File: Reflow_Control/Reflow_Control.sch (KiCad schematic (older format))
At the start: 67 parts, among them J1 Conn_5V, J2 Conn_ssr_1, J3 Conn_ssr_2, Q1 BC848, Q2 BC848, Q3 BC848, SW1 SW_Push, SW2 SW_Push, SW3 SW_Push, SW4 SW_Push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

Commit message: Kerem & Edwin dez. 20 2020 mitarbeit
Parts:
- C4: footprint PCE3853CT-ND -> Capacitor_SMD:CP_Elec_5x5.4
- H5, H6: footprint MountingHole:MountingHole_2.5mm_Pad -> owen:MountingHole_2.5mm_Pad
- SW5: footprint Rotary_Encoder:RotaryEncoder_Alps_EC11E_Vertical_H20mm -> owen:RotaryEncoder_Alps_EC11E_Vertical_H20mm
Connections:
- net BTN_A: now also U5.4 (IO0_0); no longer U5.9 (IO0_5)
- net BTN_B: now also U5.9 (IO0_5); no longer U5.10 (IO0_6)
- net BTN_CENTER: now also U5.7 (IO0_3); no longer U5.8 (IO0_4)
- net BTN_DOWN: now also U5.6 (IO0_2); no longer U5.5 (IO0_1)
- net BTN_LEFT: now also U5.5 (IO0_1); no longer U5.7 (IO0_3)
- net BTN_RIGHT: now also U5.10 (IO0_6); no longer U5.6 (IO0_2)
- net BTN_UP: now also U5.8 (IO0_4); no longer U5.4 (IO0_0)
- net INT_ENC_A: now also C10.2, R6.2, SW5.B; no longer C9.2, R5.2, SW5.A
- net INT_ENC_B: now also C9.2, R5.2, SW5.A; no longer C10.2, R6.2, SW5.B
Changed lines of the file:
@@
 EESchema Schematic File Version 4
-LIBS:Reflow_Control-cache
-EELAYER 26 0
+EELAYER 30 0
 EELAYER END
 $Descr A4 11693 8268
@@
 F 3 "" H 8500 1600 50  0001 C CNN
 	1    8500 1600
-	1    0    0    -1
-$EndComp
-$Comp
-L Device:Rotary_Encoder_Switch SW5
-U 1 1 5F6E216F
-P 10400 4350
-F 0 "SW5" H 10400 4717 50  0000 C CNN
-F 1 "Rotary_Encoder_Switch" H 10400 4626 50  0000 C CNN
-F 2 "Rotary_Encoder:RotaryEncoder_Alps_EC11E_Vertical_H20mm" H 10250 4510 50  0001 C CNN
-F 3 "~" H 10400 4610 50  0001 C CNN
-F 4 "Bourns" H 10400 4350 50  0001 C CNN "Man"
-F 5 "PEC12R-4220F-S0024" H 10400 4350 50  0001 C CNN "Man no"
-F 6 "Digikey" H 10400 4350 50  0001 C CNN "Dist"
-F 7 "PEC12R-4220F-S0024-ND" H 10400 4350 50  0001 C CNN "Dist no"
-	1    10400 4350
 	1    0    0    -1
 $EndComp
@@
 	7650 4050 7650 4150
 Connection ~ 7650 4150
+Text GLabel 1100 4400 0    50   Output ~ 0
+BTN_UP
+Text GLabel 1100 4200 0    50   Output ~ 0
+BTN_DOWN
+Text GLabel 1100 4100 0    50   Output ~ 0
+BTN_LEFT
+Text GLabel 1100 4300 0    50   Output ~ 0
+BTN_CENTER
+Text GLabel 1100 4600 0    50   Output ~ 0
+BTN_RIGHT
 Text GLabel 1100 4000 0    50   Output ~ 0
-BTN_UP
-Text GLabel 1100 4100 0    50   Output ~ 0
-BTN_DOWN
-Text GLabel 1100 4300 0    50   Output ~ 0
-BTN_LEFT
-Text GLabel 1100 4400 0    50   Output ~ 0
-BTN_CENTER
-Text GLabel 1100 4200 0    50   Output ~ 0
-BTN_RIGHT
+BTN_A
 Text GLabel 1100 4500 0    50   Output ~ 0
-BTN_A
-Text GLabel 1100 4600 0    50   Output ~ 0
 BTN_B
 $Comp
@@
 	9700 4800 9700 4900
 Connection ~ 9700 4900
+Text GLabel 9700 4150 1    50   Output ~ 0
+INT_ENC_A
 Text GLabel 9250 4150 1    50   Output ~ 0
-INT_ENC_A
-Text GLabel 9700 4150 1    50   Output ~ 0
 INT_ENC_B
 Wire Wire Line
@@
 F 0 "H5" H 10450 2046 50  0000 L CNN
 F 1 "MountingHole" H 10450 1955 50  0000 L CNN
-F 2 "MountingHole:MountingHole_2.5mm_Pad" H 10350 2000 50  0001 C CNN
+F 2 "owen:MountingHole_2.5mm_Pad" H 10350 2000 50  0001 C CNN
 F 3 "~" H 10350 2000 50  0001 C CNN
 	1    10350 2000
@@
 F 0 "H6" H 10450 2246 50  0000 L CNN
 F 1 "MountingHole" H 10450 2155 50  0000 L CNN
-F 2 "MountingHole:MountingHole_2.5mm_Pad" H 10350 2200 50  0001 C CNN
+F 2 "owen:MountingHole_2.5mm_Pad" H 10350 2200 50  0001 C CNN
 F 3 "~" H 10350 2200 50  0001 C CNN
 	1    10350 2200
@@
 F 0 "C4" H 6141 4246 50  0000 L CNN
 F 1 "100uF" H 6141 4155 50  0000 L CNN
-F 2 "PCE3853CT-ND" H 6050 4200 50  0001 C CNN
+F 2 "Capacitor_SMD:CP_Elec_5x5.4" H 6050 4200 50  0001 C CNN
 F 3 "~" H 6050 4200 50  0001 C CNN
 F 4 "Panasonic" H 6050 4200 50  0001 C CNN "Man"
@@
 Wire Wire Line
 	3750 750  3850 750
+$Comp
+L Device:Rotary_Encoder_Switch SW5
+U 1 1 5F6E216F
+P 10400 4350
+F 0 "SW5" H 10400 4717 50  0000 C CNN
+F 1 "Rotary_Encoder_Switch" H 10400 4626 50  0000 C CNN
+F 2 "owen:RotaryEncoder_Alps_EC11E_Vertical_H20mm" H 10250 4510 50  0001 C CNN
+F 3 "~" H 10400 4610 50  0001 C CNN
+F 4 "Bourns" H 10400 4350 50  0001 C CNN "Man"
+F 5 "PEC12R-4220F-S0024" H 10400 4350 50  0001 C CNN "Man no"
+F 6 "Digikey" H 10400 4350 50  0001 C CNN "Dist"
+F 7 "PEC12R-4220F-S0024-ND" H 10400 4350 50  0001 C CNN "Dist no"
+	1    10400 4350
+	1    0    0    -1
+$EndComp
 $EndSCHEMATC

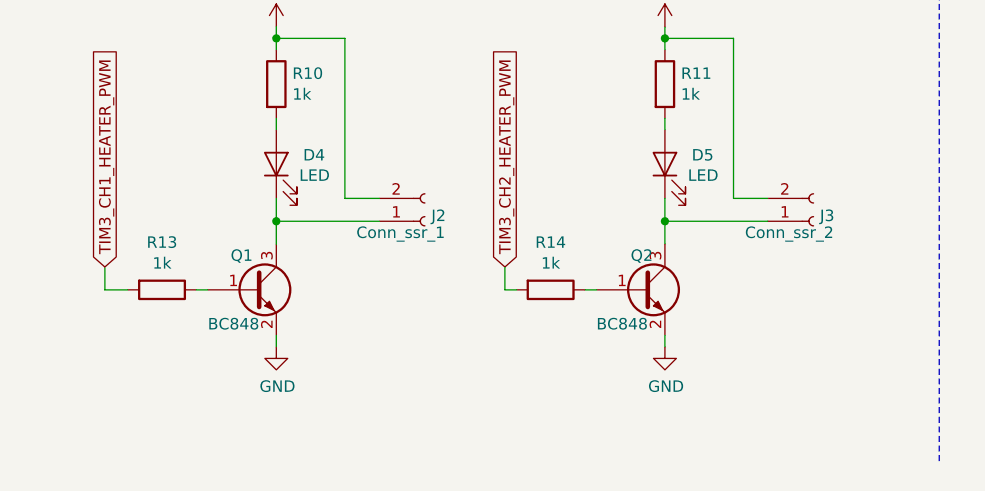
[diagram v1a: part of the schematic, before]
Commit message: repaced NPN with nud3112 relay switcher
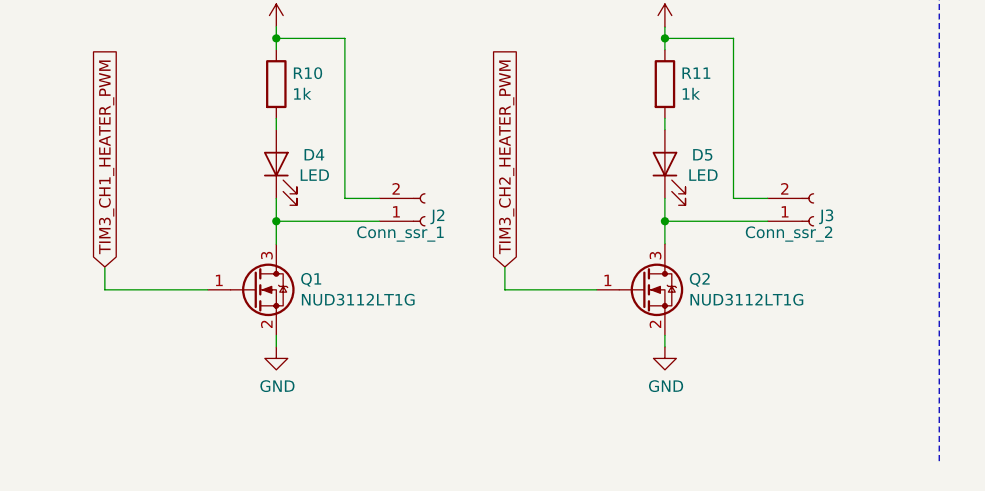
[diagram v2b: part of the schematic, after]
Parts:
- removed Q1, Q2: BC848, Package_TO_SOT_SMD:SOT-23, symbol Transistor_BJT:BC848
- removed R13, R14: 1k, Resistor_SMD:R_1206_3216Metric_Pad1.42x1.75mm_HandSolder, symbol Device:R
- added Q1, Q2: NUD3112LT1G, Package_TO_SOT_SMD:SOT-23_Handsoldering, symbol Device:Q_NMOS_GSD
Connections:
- net GND: now also Q1.2 (S), Q2.2 (S)
- net TIM3_CH1_HEATER_PWM: now also Q1.1 (G)
- net TIM3_CH2_HEATER_PWM: now also Q2.1 (G)
- net at D4.1 (K), J2.1 (Pin_1): now also Q1.3 (D)
- net at D5.1 (K), J3.1 (Pin_1): now also Q2.3 (D)
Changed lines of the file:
@@
 $EndComp
-$Comp
-L Device:R R13
-U 1 1 5FE63CBF
-P 1050 7000
-F 0 "R13" V 843 7000 50  0000 C CNN
-F 1 "1k" V 934 7000 50  0000 C CNN
-F 2 "Resistor_SMD:R_1206_3216Metric_Pad1.42x1.75mm_HandSolder" V 980 7000 50  0001 C CNN
-F 3 "~" H 1050 7000 50  0001 C CNN
-F 4 "Rhom" H 1050 7000 50  0001 C CNN "Man"
-F 5 "KTR18EZPF1001" H 1050 7000 50  0001 C CNN "Man no"
-F 6 "Digikey" H 1050 7000 50  0001 C CNN "Dist"
-F 7 "RHM1.00KAICT-ND" H 1050 7000 50  0001 C CNN "Dist no"
-	1    1050 7000
-	0    1    1    0
-$EndComp
-Wire Wire Line
-	1200 7000 1250 7000
 $Comp
 L Device:R R10
@@
 	800  6900 800  7000
 Wire Wire Line
-	800  7000 900  7000
-Wire Wire Line
 	1550 5850 1550 5900
-$Comp
-L Transistor_BJT:BC848 Q2
-U 1 1 5FF3250B
-P 3150 7000
-F 0 "Q2" H 3100 7150 50  0000 L CNN
-F 1 "BC848" H 2950 6850 50  0000 L CNN
-F 2 "Package_TO_SOT_SMD:SOT-23" H 3350 6925 50  0001 L CIN
-F 3 "http://www.infineon.com/dgdl/Infineon-BC847SERIES_BC848SERIES_BC849SERIES_BC850SERIES-DS-v01_01-en.pdf?fileId=db3a304314dca389011541d4630a1657" H 3150 7000 50  0001 L CNN
-F 4 "Nexperia" H 3150 7000 50  0001 C CNN "Man"
-F 5 "BC848B,215" H 3150 7000 50  0001 C CNN "Man no"
-F 6 "Digikey" H 3150 7000 50  0001 C CNN "Dist"
-F 7 "1727-4241-1-ND" H 3150 7000 50  0001 C CNN "Dist no"
-	1    3150 7000
-	1    0    0    -1
-$EndComp
 $Comp
 L power:GND #PWR041
@@
 Wire Wire Line
 	3250 7250 3250 7200
-$Comp
-L Device:R R14
-U 1 1 5FF3251E
-P 2750 7000
-F 0 "R14" V 2543 7000 50  0000 C CNN
-F 1 "1k" V 2634 7000 50  0000 C CNN
-F 2 "Resistor_SMD:R_1206_3216Metric_Pad1.42x1.75mm_HandSolder" V 2680 7000 50  0001 C CNN
-F 3 "~" H 2750 7000 50  0001 C CNN
-F 4 "Rhom" H 2750 7000 50  0001 C CNN "Man"
-F 5 "KTR18EZPF1001" H 2750 7000 50  0001 C CNN "Man no"
-F 6 "Digikey" H 2750 7000 50  0001 C CNN "Dist"
-F 7 "RHM1.00KAICT-ND" H 2750 7000 50  0001 C CNN "Dist no"
-	1    2750 7000
-	0    1    1    0
-$EndComp
-Wire Wire Line
-	2900 7000 2950 7000
 $Comp
 L Device:R R11
@@
 Wire Wire Line
 	2550 6900 2550 7000
-Wire Wire Line
-	2550 7000 2600 7000
 Wire Wire Line
 	3250 5850 3250 5900
@@
 	3250 6700 3250 6800
 Connection ~ 1550 6700
-$Comp
-L Transistor_BJT:BC848 Q1
-U 1 1 5FE63CA8
-P 1450 7000
-F 0 "Q1" H 1350 7150 50  0000 L CNN
-F 1 "BC848" H 1250 6850 50  0000 L CNN
-F 2 "Package_TO_SOT_SMD:SOT-23" H 1650 6925 50  0001 L CIN
-F 3 "http://www.infineon.com/dgdl/Infineon-BC847SERIES_BC848SERIES_BC849SERIES_BC850SERIES-DS-v01_01-en.pdf?fileId=db3a304314dca389011541d4630a1657" H 1450 7000 50  0001 L CNN
-F 4 "Nexperia" H 1450 7000 50  0001 C CNN "Man"
-F 5 "BC848B,215" H 1450 7000 50  0001 C CNN "Man no"
-F 6 "Digikey" H 1450 7000 50  0001 C CNN "Dist"
-F 7 "1727-4241-1-ND" H 1450 7000 50  0001 C CNN "Dist no"
-	1    1450 7000
-	1    0    0    -1
-$EndComp
 Wire Wire Line
 	1550 7200 1550 7250
@@
 	1    0    0    -1
 $EndComp
+$Comp
+L Device:Q_NMOS_GSD Q1
+U 1 1 602ABD20
+P 1450 7000
+F 0 "Q1" H 1655 7046 50  0000 L CNN
+F 1 "NUD3112LT1G" H 1655 6955 50  0000 L CNN
+F 2 "Package_TO_SOT_SMD:SOT-23_Handsoldering" H 1650 7100 50  0001 C CNN
+F 3 "~" H 1450 7000 50  0001 C CNN
+F 4 "On Semi" H 1450 7000 50  0001 C CNN "Man"
+F 5 "NUD3112LT1G" H 1450 7000 50  0001 C CNN "Man no"
+F 6 "Digikey" H 1450 7000 50  0001 C CNN "Disti"
+F 7 "NUD3112LT1GOSCT-ND" H 1450 7000 50  0001 C CNN "Disti no"
+	1    1450 7000
+	1    0    0    -1
+$EndComp
+Wire Wire Line
+	800  7000 1250 7000
+Wire Wire Line
+	2550 7000 2950 7000
+$Comp
+L Device:Q_NMOS_GSD Q2
+U 1 1 602CF91F
+P 3150 7000
+F 0 "Q2" H 3355 7046 50  0000 L CNN
+F 1 "NUD3112LT1G" H 3355 6955 50  0000 L CNN
+F 2 "Package_TO_SOT_SMD:SOT-23_Handsoldering" H 3350 7100 50  0001 C CNN
+F 3 "~" H 3150 7000 50  0001 C CNN
+F 4 "On Semi" H 3150 7000 50  0001 C CNN "Man"
+F 5 "NUD3112LT1G" H 3150 7000 50  0001 C CNN "Man no"
+F 6 "Digikey" H 3150 7000 50  0001 C CNN "Disti"
+F 7 "NUD3112LT1GOSCT-ND" H 3150 7000 50  0001 C CNN "Disti no"
+	1    3150 7000
+	1    0    0    -1
+$EndComp

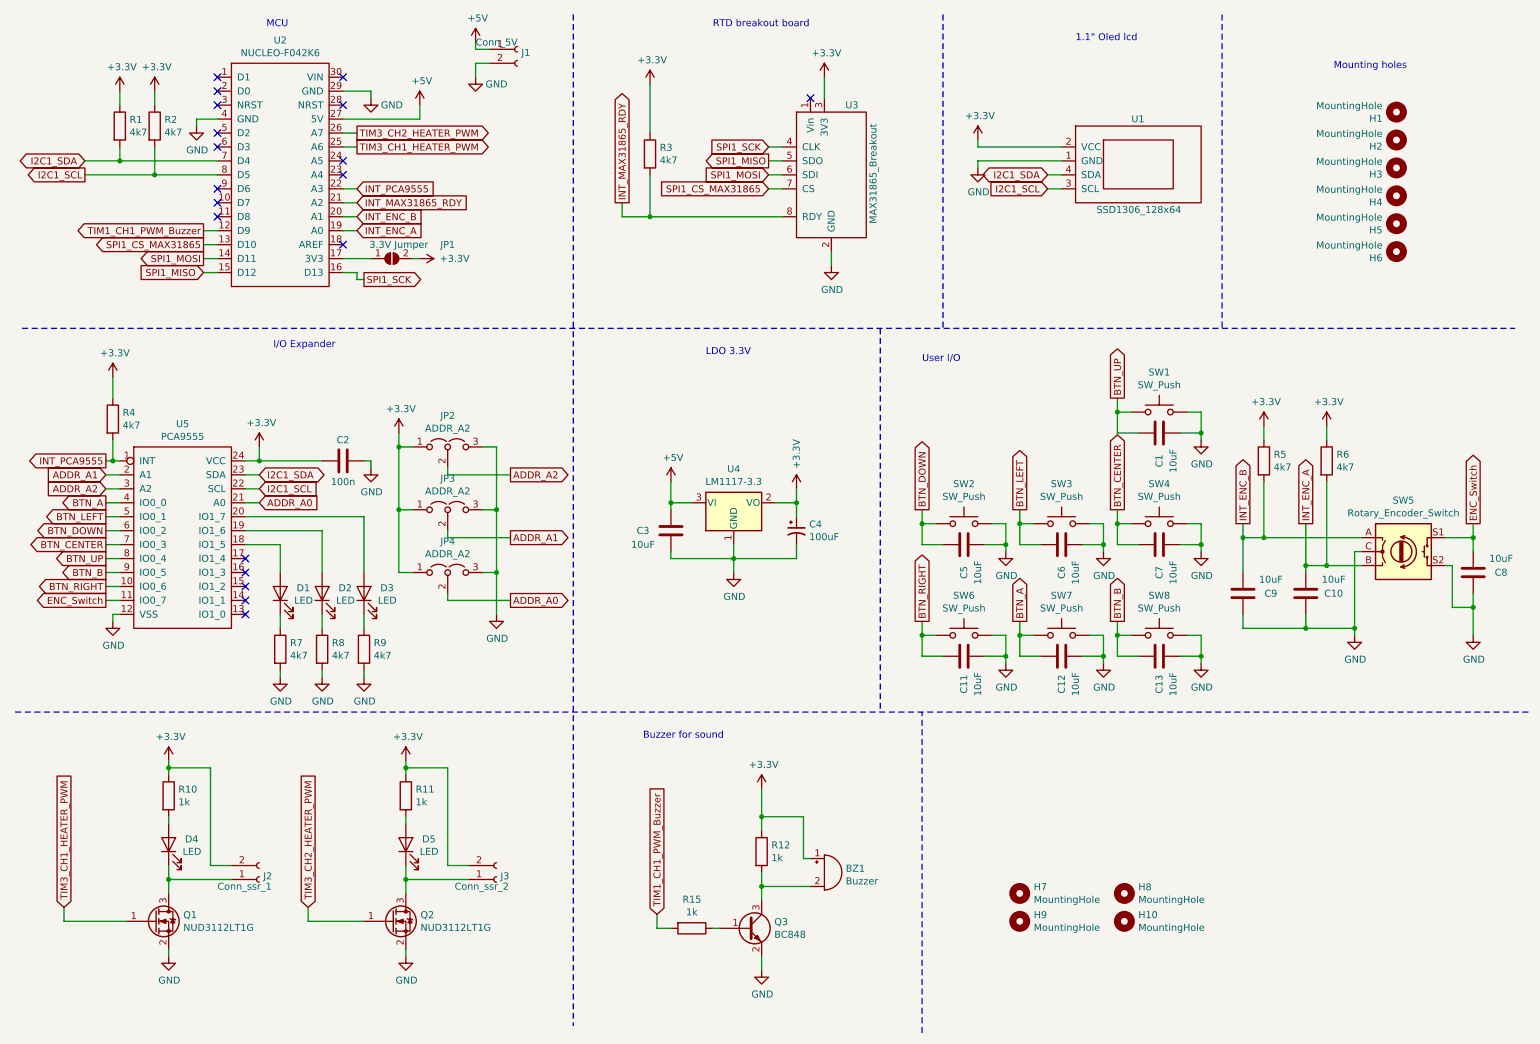
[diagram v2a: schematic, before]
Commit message: added motor controller
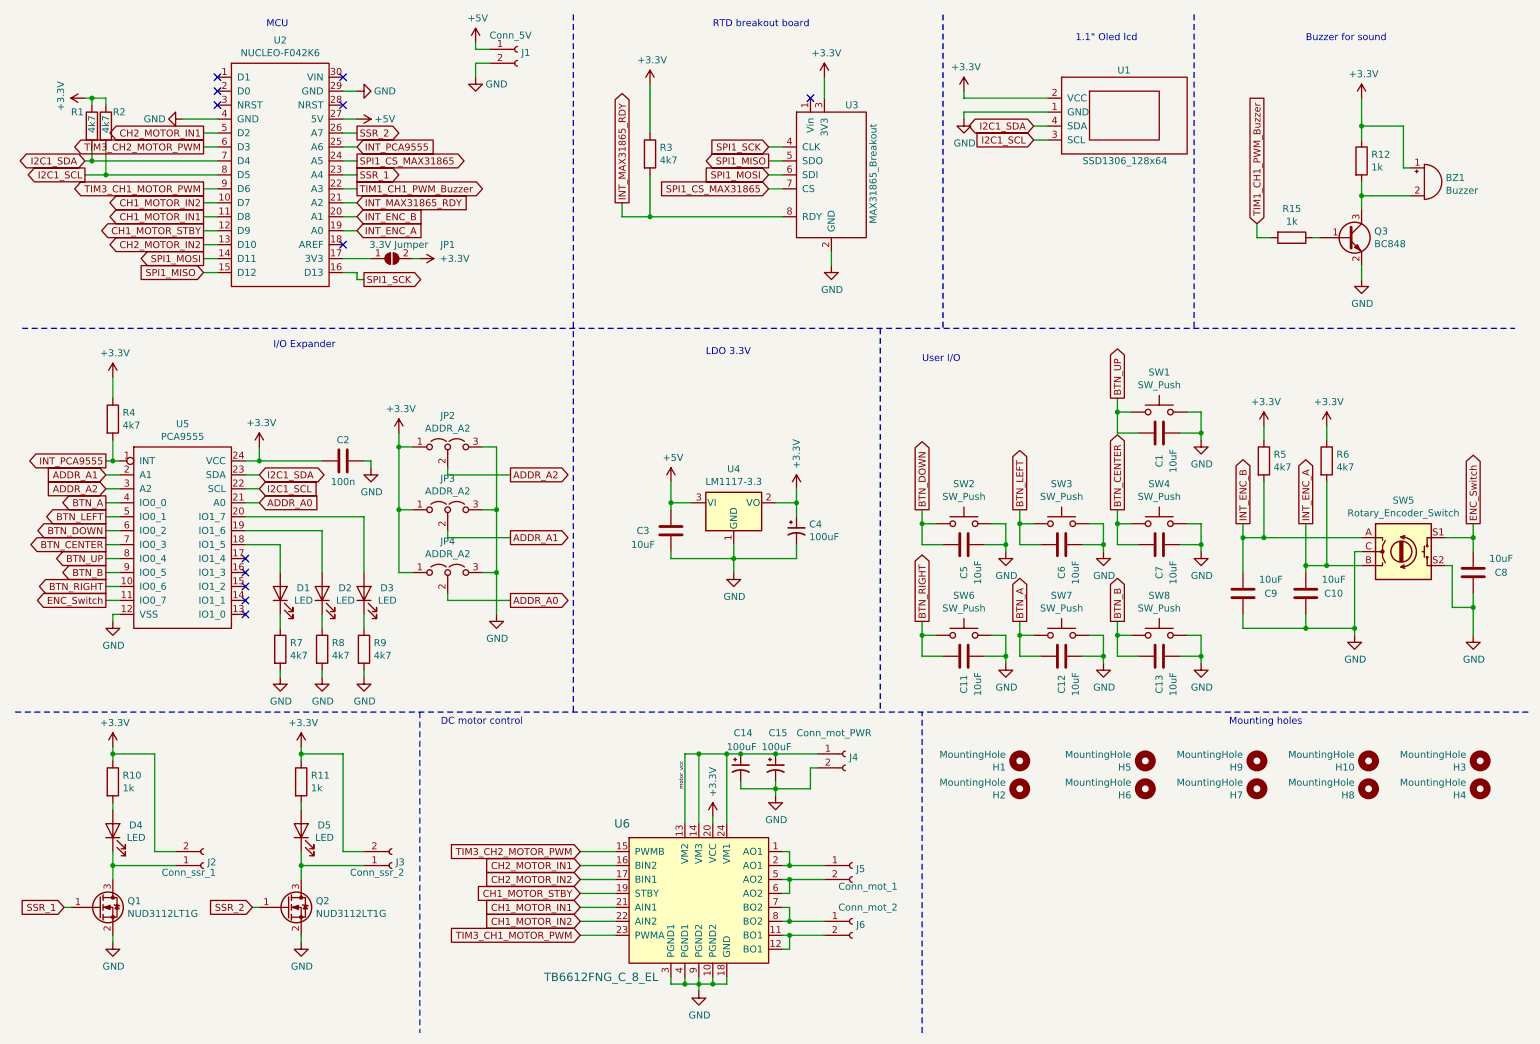
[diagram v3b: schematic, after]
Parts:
- added C14, C15: 100uF, Capacitor_SMD:CP_Elec_8x6.2, symbol Device:CP1_Small
- added J4: Conn_mot_PWR, Connector_Phoenix_MC_HighVoltage:PhoenixContact_MC_1,5_2-G-5.08_1x02_P5.08mm_Horizontal, symbol Connector:Conn_01x02_Female
- added J5: Conn_mot_1, Connector_Phoenix_MC_HighVoltage:PhoenixContact_MC_1,5_2-G-5.08_1x02_P5.08mm_Horizontal, symbol Connector:Conn_01x02_Female
- added J6: Conn_mot_2, Connector_Phoenix_MC_HighVoltage:PhoenixContact_MC_1,5_2-G-5.08_1x02_P5.08mm_Horizontal, symbol Connector:Conn_01x02_Female
- added U6: TB6612FNG_C_8_EL, dk_footprints:LSSOP-24_W5.6mm, symbol dk_PMIC-Motor-Drivers-Controllers:TB6612FNG_C_8_EL
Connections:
- net +3V3: now also U6.20 (VCC)
- net GND: now also C14.2, C15.2, J4.2 (Pin_2), U6.10 (PGND2), U6.18 (GND), U6.3 (PGND1), U6.4 (PGND1), U6.9 (PGND2)
- net INT_PCA9555: now also U2.25 (A6); no longer U2.22 (A3)
- net SPI1_CS_MAX31865: now also U2.24 (A5); no longer U2.13 (D10)
- net TIM1_CH1_PWM_Buzzer: now also U2.22 (A3); no longer U2.12 (D9)
- net CH1_MOTOR_IN2: now reaches U2.10 (D7)
- net CH1_MOTOR_IN2: now also U6.22 (AIN2)
- net CH1_MOTOR_IN1: now reaches U2.11 (D8)
- net CH1_MOTOR_IN1: now also U6.21 (AIN1)
- net SSR_1: now reaches U2.23 (A4)
- net SSR_1: now also Q1.1 (G)
- net CH2_MOTOR_IN1: now reaches U2.5 (D2)
- net CH2_MOTOR_IN1: now also U6.16 (BIN2)
- net TIM3_CH2_MOTOR_PWM: now reaches U2.6 (D3)
- net TIM3_CH2_MOTOR_PWM: now also U6.15 (PWMB)
- net TIM3_CH1_MOTOR_PWM: now reaches U2.9 (D6)
- net TIM3_CH1_MOTOR_PWM: now also U6.23 (PWMA)
- removed net TIM3_CH1_HEATER_PWM: Q1.1 (G), U2.25 (A6)
- net TIM3_CH2_HEATER_PWM renamed SSR_2
- new net: J5.1 (Pin_1), U6.1 (AO1), U6.2 (AO1)
- new net: J6.2 (Pin_2), U6.11 (BO1), U6.12 (BO1)
- new net: J5.2 (Pin_2), U6.5 (AO2), U6.6 (AO2)
- new net: J6.1 (Pin_1), U6.7 (BO2), U6.8 (BO2)
- new net CH1_MOTOR_STBY: U2.12 (D9), U6.19 (STBY)
- new net CH2_MOTOR_IN2: U2.13 (D10), U6.17 (BIN1)
- new net motor_vcc: C14.1, C15.1, J4.1 (Pin_1), U6.13 (VM2), U6.14 (VM3), U6.24 (VM1)
- no-connect marks 19 -> 12
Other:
- note added: "DC motor control"
- moved on the sheet: BZ1, D4, D5, H1, H10, H2, H3, H4, H5, H6, H7, H8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
